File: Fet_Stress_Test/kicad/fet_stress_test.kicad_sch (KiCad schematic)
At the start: 12 parts

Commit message: Uploading Evil Schemes
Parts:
- removed D?: Green, LED_THT:LED_D5.0mm, symbol Device:LED
- removed D?: Yellow, LED_THT:LED_D5.0mm, symbol Device:LED
- removed D?: 824500241, Diode_SMD:D_SMA, symbol Device:D_Zener
- removed D?: 14V, Diode_SMD:D_SOD-123, symbol Device:D_Zener
- removed Q?: (no value), symbol Transistor_FET:IRF9540N
- removed Q?: MMBT3904, Package_TO_SOT_SMD:SOT-23, symbol Transistor_BJT:MMBT3904
- removed R? (x5): 1K, Resistor_SMD:R_0603_1608Metric_Pad0.98x0.95mm_HandSolder, symbol Device:R_US
- removed R?: 2.2K, Resistor_SMD:R_0603_1608Metric_Pad0.98x0.95mm_HandSolder, symbol Device:R_US
- added D?: 824500241, Diode_SMD:D_SMA, symbol Device:D_Zener
- added D?: Green, LED_THT:LED_D5.0mm, symbol Device:LED
- added D?: 14V, Diode_SMD:D_SOD-123, symbol Device:D_Zener
- added D?: Yellow, LED_THT:LED_D5.0mm, symbol Device:LED
- added Q?: MMBT3904, Package_TO_SOT_SMD:SOT-23, symbol Transistor_BJT:MMBT3904
- added Q?: ~, symbol Transistor_FET:IRF9540N
- added R? (x5): 1K, Resistor_SMD:R_0603_1608Metric_Pad0.98x0.95mm_HandSolder, symbol Device:R_US
- added R?: 2.2K, Resistor_SMD:R_0603_1608Metric_Pad0.98x0.95mm_HandSolder, symbol Device:R_US
- added TP? (x2): TestPoint, TestPoint:TestPoint_THTPad_D1.5mm_Drill0.7mm, symbol Connector:TestPoint
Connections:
- net GND: now also D?.1 (K), D?.1 (K), D?.2 (A), Q?.2 (D), Q?.2 (E), R?.1, TP?.1, TP?.1
- new net: R?.1, R?.2 (x2)
- new net: D?.2 (A), R?.2 (x2)
- new net: Q?.1 (B), R?.1
- new net: D?.1 (K), D?.2 (A), Q?.3 (C)
- new net: D?.1 (K), Q?.1 (G), R?.2
- new net: Q?.3 (S), R?.1, R?.1
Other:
- note added: "PCB Resistor"
- note added: "Sorry Jacob no aluminum pcb. I want to test the thermal performance of the fet near max load. Need same pcb characteristsics for that."
- note added: "The purpose of this board will be to serve as a cheap dummy load allowing us to test the limits of the fet output channels on our test stand with a much cheaper PCB"
- note added: "This is going to be a fun board heh"
- company: Missouri S&T Rocket Design Team -> Missouri S&T RDT
- title: DOM - Fet Output Channel -> Fet Stress Test

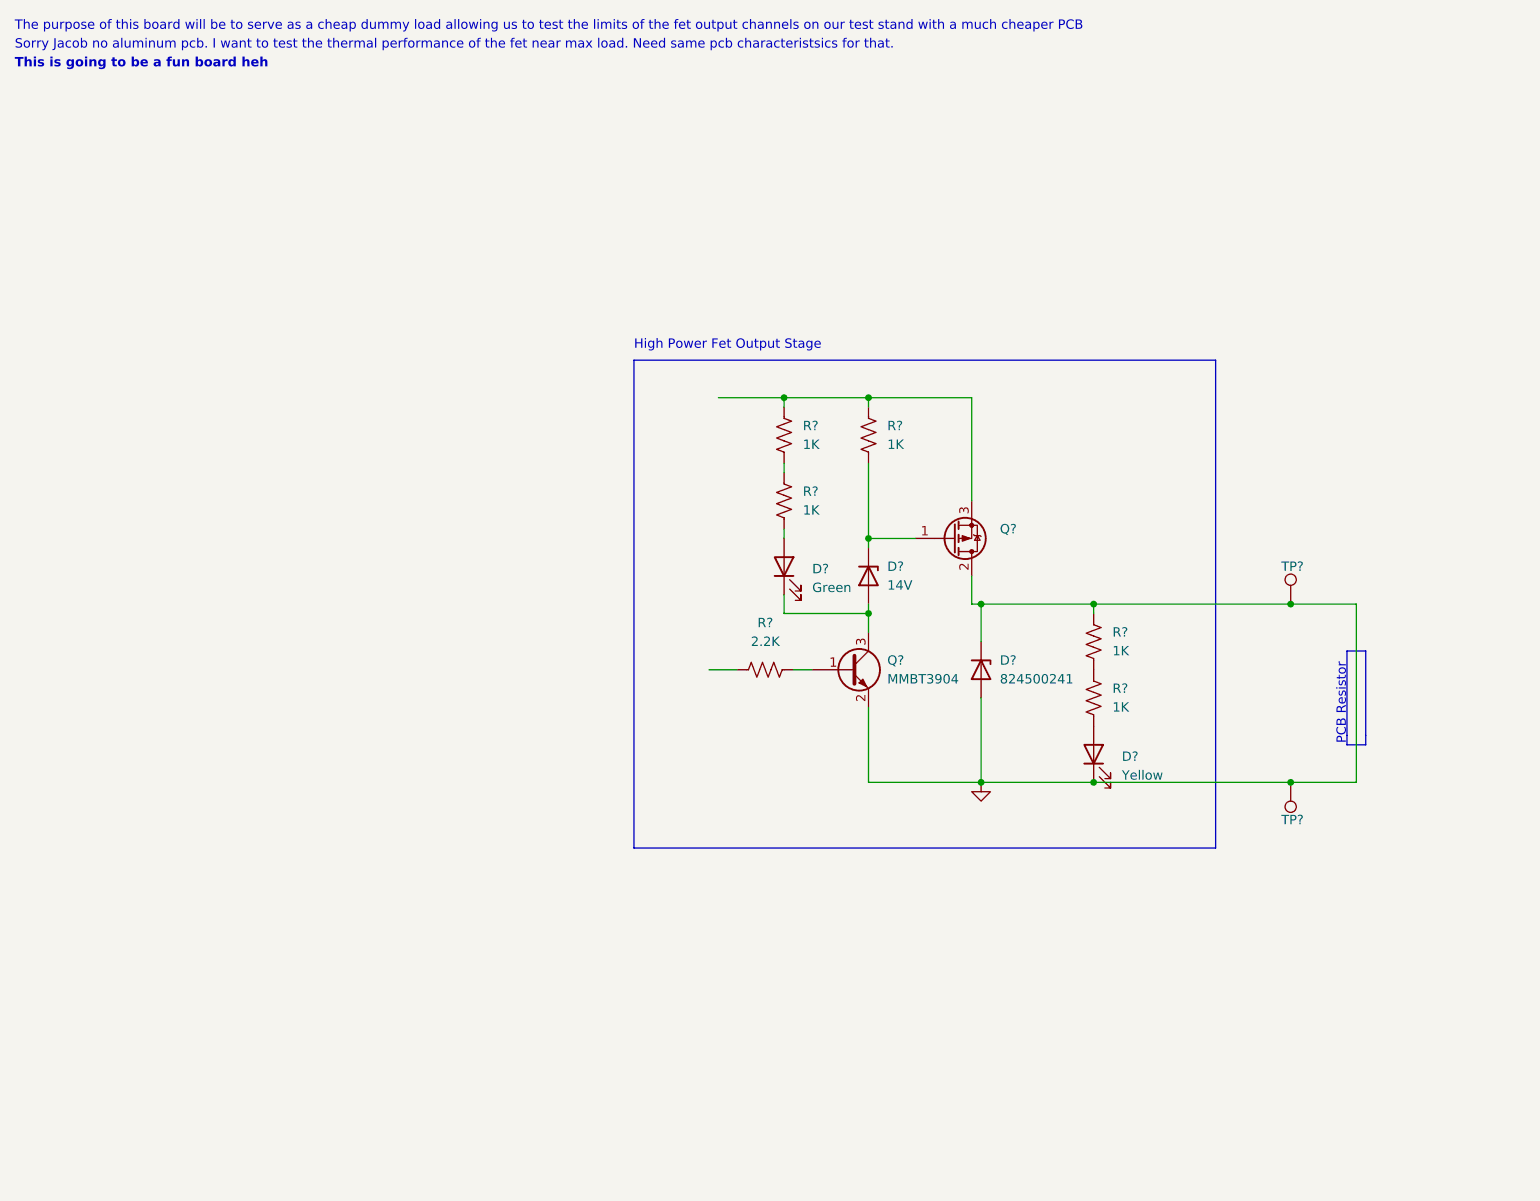
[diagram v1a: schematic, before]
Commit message: started work routing fet stress
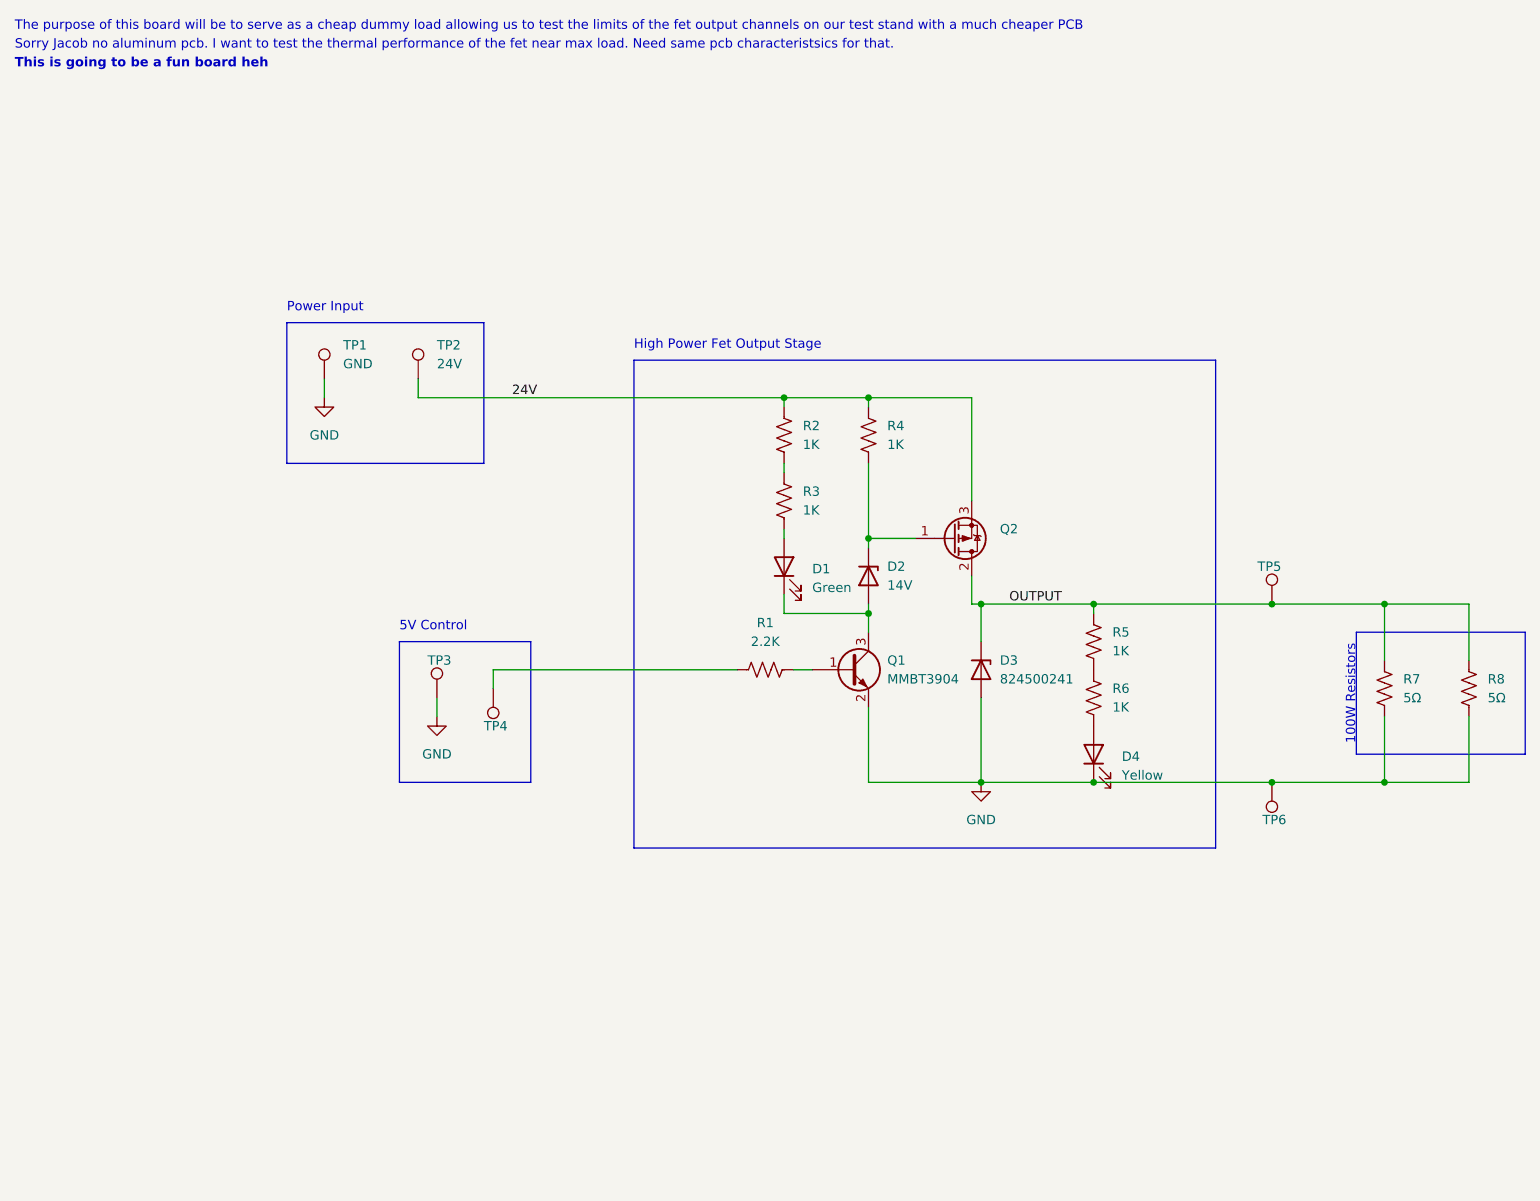
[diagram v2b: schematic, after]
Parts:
- added R7, R8: 5Ω, Package_TO_SOT_THT:TO-247-2_Horizontal_TabDown, symbol Device:R_US
- added TP1: GND, DOM:15x15mm_pad, symbol Connector:TestPoint
- added TP2: 24V, DOM:15x15mm_pad, symbol Connector:TestPoint
- added TP5, TP6: TestPoint, TestPoint:TestPoint_THTPad_D1.5mm_Drill0.7mm, symbol Connector:TestPoint
- Q2: renamed from Q?; footprint (none) -> DOM:TO-220F-3_Horizontal_TabDown_SMD_PAD
- gave numbers to parts that had none: 13
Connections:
- net GND: now also R7.2, R8.1, TP1.1, TP6.1; no longer D3.1 (K), Q2.2 (D), R5.1, TP4.1
- net 24V: now reaches Q2.3 (S), R2.1, R4.1
- net 24V: now also TP2.1
- net at R1.2: now also TP4.1
- new net OUTPUT: D3.1 (K), Q2.2 (D), R5.1, R7.1, R8.2, TP5.1
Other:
- note added: "100W Resistors"
- note added: "5V Control"
- note added: "Power Input"
- note removed: "PCB Resistor"
- moved on the sheet: TP3, TP4

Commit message: Finalized footprints and regenerated gerbers, added BOM
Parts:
- added J1: GX_16-2, DOM:GX_16-2, symbol Connector_Generic:Conn_01x02
- added J2: GX_16-3, DOM:GX_16-3, symbol Connector_Generic:Conn_01x03
- added J3: GX_16-4, DOM:GX_16-4, symbol Connector_Generic:Conn_01x04
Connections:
- net GND: now also J1.1 (Pin_1), J1.2 (Pin_2), J2.1 (Pin_1), J2.2 (Pin_2), J2.3 (Pin_3), J3.1 (Pin_1), J3.2 (Pin_2), J3.3 (Pin_3), J3.4 (Pin_4)
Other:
- note added: "Test Footprints"
